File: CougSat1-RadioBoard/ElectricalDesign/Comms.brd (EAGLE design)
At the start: 91.4 x 95.8 mm, 427 parts, among them J1 230mm Antenna, J2 CougSat Card, J3 230mm Antenna, J4 SWD, Q1 CSD25402Q3A, Q10 MMBTA06W, Q11 MMBTA06W, Q12 DMN53D0LDW, Q13 DMP2065UFDB, Q14 MMBTA06W, Q15 CSD25402Q3A, Q16 CSD25402Q3A, Q2 CSD25402Q3A, Q3 CSD25402Q3A, Q4 DMN53D0LDW, Q5 CSD25402Q3A, Q6 CSD25402Q3A, Q7 CSD25402Q3A, Q8 DMN53D0LDW, Q9 DMN53D0LDW, U1 TPS73250, U10 MAAP-011232, U11 LTC2499, U12 LTC2499, U13 LTC2499, U14 LP5907MFX-3.1, U15 TPS73250, U16 AD8137, U17 STM32L496RGT, U18 AD8137, U19 MAAP-011232, U2 LP5907MFX-3.1, U20 ADF4360, U21 HMC545A, U22 AD8515, U23 MAAM-011229, U24 AD8515, U25 MAAM-011229, U26 AD8345, U27 LM2776, U28 AD8348, U29 MCP1501-18, U3 TPS61236, U30 TXS0102DQM, U31 MAAM-011229, U32 AD8515, U33 AD8515, U34 AD8515, U35 TXS0102DQM, U36 ADF4360, U37 AD8515, U38 AD8515, U39 AD8515, U4 AD8346, U40 AD8515, U41 AD8137, U42 AD8137, U43 LP5907MFX-3.1, U44 TPS73250, U5 ADF4360, U6 TPS61089, U7 MAAM-011229, U8 IS25LP016D, U9 IS25LP016D, Y1 20MHz ±2.5ppm, Y2 32.768kHz ±10ppm, Y3 16MHz ±10ppm, Y4 20MHz ±2.5ppm, Y5 20MHz ±2.5ppm

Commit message: Updated mCAD
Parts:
- removed R116, R117, R118: 10kΩ 0.1%, CougsInSpace-Resistors:1608
- removed R119, R120, R121: 1.2kΩ 0.1%, CougsInSpace-Resistors:1608
- removed R122: 0Ω <20mΩ, CougsInSpace-Resistors:1608
- removed R123, R124: 50mΩ 1%, CougsInSpace-Resistors:1608
- removed R125: 1kΩ 0.1%, CougsInSpace-Resistors:1608
- removed R126, R127, R128: 5kΩ 0.1%, CougsInSpace-Resistors:1616
- added RN1, RN5, RN6: 50kΩ 0.1%, CougsInSpace-Resistors:1616
- added RN10, RN2, RN3, RN4, RN7, RN8, RN9: 20kΩ 0.1%, CougsInSpace-Resistors:1616
- added RN11, RN12, RN13: 5kΩ 0.1%, CougsInSpace-Resistors:1616
- R100: value 1kΩ 0.1% -> 10kΩ 0.1%
- R101, R102, R103: value 100kΩ 0.1% -> 10kΩ 0.1%
- R104: value 13.7kΩ 0.1% -> 10kΩ 0.1%
- R105, R106, R107, R108, R66: value 3.3kΩ 0.1% -> 10kΩ 0.1%
- R110, R111: value 10kΩ 0.1% -> 1.2kΩ 0.1%
- R112, R33, R41, R46: value 10kΩ 0.1% -> 0Ω <20mΩ
- R113, R114, R37: value 10kΩ 0.1% -> 50mΩ 1%
- R115: value 10kΩ 0.1% -> 1kΩ 0.1%
- R24, R32: value 50kΩ 0.1% -> 0Ω <20mΩ; device CougsInSpace-Resistors:1616 -> CougsInSpace-Resistors:1608
- R25: value 0Ω <20mΩ -> 4.7kΩ 0.1%
- R26, R29, R30, R36: value 20kΩ 0.1% -> 10kΩ 0.1%; device CougsInSpace-Resistors:1616 -> CougsInSpace-Resistors:1608
- R27: value 4.7kΩ 0.1% -> 50mΩ 1%
- R31: value 50mΩ 1% -> 10kΩ 0.1%
- R35: value 50kΩ 0.1% -> 10kΩ 0.1%; device CougsInSpace-Resistors:1616 -> CougsInSpace-Resistors:1608
- R38, R39: value 20kΩ 0.1% -> 50mΩ 1%; device CougsInSpace-Resistors:1616 -> CougsInSpace-Resistors:1608
- R40: value 20kΩ 0.1% -> 0Ω <20mΩ; device CougsInSpace-Resistors:1616 -> CougsInSpace-Resistors:1608
- R42, R56: value 0Ω <20mΩ -> 3.3kΩ 0.1%
- R43, R50, R51, R67, R81: value 0Ω <20mΩ -> 2kΩ 0.1%
- R44, R87: value 10kΩ 0.1% -> 100kΩ 0.1%
- R45: value 10kΩ 0.1% -> 820kΩ 1%
- R47: value 50mΩ 1% -> 100kΩ 0.1%
- R48: value 50mΩ 1% -> 820kΩ 1%
- R49: value 50mΩ 1% -> 3.3kΩ 0.1%
- R53: value 2kΩ 0.1% -> 1kΩ 0.1%
- R54: value 100kΩ 0.1% -> 13.7kΩ 0.1%
- R55: value 820kΩ 1% -> 2kΩ 0.1%
- R57: value 100kΩ 0.1% -> 0Ω <20mΩ
- R58: value 820kΩ 1% -> 200kΩ 0.1%
- R59: value 3.3kΩ 0.1% -> 49.9Ω 0.1%
- R60: value 2kΩ 0.1% -> 49.9Ω 0.1%
- R61: value 2kΩ 0.1% -> 4.7kΩ 0.1%
- R62: value 3.3kΩ 0.1% -> 0Ω <20mΩ
- R63: value 1kΩ 0.1% -> 2kΩ 0.1%
- R64: value 13.7kΩ 0.1% -> 470Ω 0.5%
- R65, R89, R91: value 2kΩ 0.1% -> 100kΩ 0.1%
- R68: value 200kΩ 0.1% -> 2kΩ 0.1%
- R69, R85: value 49.9Ω 0.1% -> 470Ω 0.5%
- R70: value 49.9Ω 0.1% -> 2kΩ 0.1%
- R71: value 4.7kΩ 0.1% -> 0Ω <20mΩ
- R72: value 0Ω <20mΩ -> 10kΩ 0.1%
- R73, R77: value 2kΩ 0.1% -> 10kΩ 0.1%
- R74: value 470Ω 0.5% -> 10kΩ 0.1%
- R75: value 100kΩ 0.1% -> 49.9Ω 0.1%
- R76: value 10kΩ 0.1% -> 20kΩ 0.5%
- R78: value 2kΩ 0.1% -> 60.4Ω 0.1%
- R79: value 470Ω 0.5% -> 2kΩ 0.1%
- R80: value 2kΩ 0.1% -> 316kΩ 0.1%
- R82: value 10kΩ 0.1% -> 49.9Ω 0.1%
- R83: value 10kΩ 0.1% -> 470Ω 0.5%
- R84: value 10kΩ 0.1% -> 4.7kΩ 0.1%
- R86: value 20kΩ 0.5% -> 200kΩ 0.1%
- R88: value 60.4Ω 0.1% -> 100kΩ 0.1%
- R90: value 316kΩ 0.1% -> 1kΩ 0.1%
- R92: value 49.9Ω 0.1% -> 100kΩ 0.1%
- R93: value 470Ω 0.5% -> 100kΩ 0.1%
- R94: value 4.7kΩ 0.1% -> 13.7kΩ 0.1%
- R95: value 470Ω 0.5% -> 3.3kΩ 0.1%
- R96: value 200kΩ 0.1% -> 3.3kΩ 0.1%
- R97, R98: value 100kΩ 0.1% -> 3.3kΩ 0.1%
- R99: value 100kΩ 0.1% -> 1.2kΩ 0.1%
- moved R63 82.3 mm to (88.3, -16.2)
- moved R80 68.6 mm to (18.3, -25.0), turned to 0 degrees
- moved R67 61.8 mm to (69.1, -17.1)
- moved R100 59.6 mm to (70.0, -38.9), turned to 180 degrees
- moved R82 59.6 mm to (86.9, -25.5), turned to 180 degrees
- moved R57 59.0 mm to (7.50, -12.1), turned to 90 degrees
- moved R92 57.8 mm to (29.5, -31.9), turned to 270 degrees
- moved R73 56.2 mm to (32.2, -19.3), turned to 90 degrees
- moved R95 55.6 mm to (23.7, -34.5)
- moved R75 54.0 mm to (87.4, -20.1)
- moved R33 52.1 mm to (75.7, 10.6), turned to 180 degrees
- moved R83 51.5 mm to (83.3, -26.0), turned to 180 degrees
- moved R104 51.5 mm to (35.4, -40.4), turned to 270 degrees
- moved R114 49.8 mm to (85.2, -42.2), turned to 180 degrees
- moved R42 49.7 mm to (35.9, -1.50), turned to 180 degrees
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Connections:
- net !NRST: now also R62.1; no longer R72.1
- net 3.3V: now also R100.2, R28.2, R29.2, R30.2, R31.2, R36.2, R53.2, R66.2, R72.2; no longer R110.2, R33.2, R34.2, R37.2, R41.2, R46.2, R63.2, R76.2, R82.2
- net 3.3V_1: now also R75.2, R82.2; no longer R85.2, R92.2
- net 3.3V_2: now also R59.2, R60.2; no longer R69.2, R70.2
- net 5.0V: now also RN2.3; no longer R26.3
- net 5.0V_1: now also R63.2; no longer R73.2
- net 5.0V_2: now also R67.2, R81.2; no longer R77.2, R91.2
- net 5.0V_I: now also RN2.4; no longer R26.4
- net 9.0V: now also RN1.4; no longer R24.4
- net 9.0V_0: now also R27.2, RN5.3; no longer R31.2, R32.3
- net 9.0V_1: now also R39.2, R44.2, R47.2, RN6.4; no longer R35.4, R49.2, R54.2, R57.2
- net 9.0V_I: now also RN1.3; no longer R24.3
- net ADC_5.0V: now also RN2.2; no longer R26.2
- net ADC_5.0V_I: now also RN2.1; no longer R26.1
- net ADC_9.0V: now also RN1.1; no longer R24.1
- net ADC_9.0V_0: now also RN5.2; no longer R32.2
- net ADC_9.0V_1: now also RN6.1; no longer R35.1
- net ADC_9.0V_I: now also RN1.2; no longer R24.2
- net ADC_ADCINN-0: now also RN12.4, RN8.1; no longer R127.4, R38.1
- net ADC_ADCINN-1: now also RN13.4, RN3.1; no longer R128.4, R29.1
- net ADC_ADCINN-2: now also RN10.1, RN11.4; no longer R126.4, R40.1
- net ADC_ADCINP-0: now also RN12.3, RN8.2; no longer R127.3, R38.2
- net ADC_ADCINP-1: now also RN13.3, RN3.2; no longer R128.3, R29.2
- net ADC_ADCINP-2: now also RN10.2, RN11.3; no longer R126.3, R40.2
- net ADC_I_5.0V-0N: now also RN4.1; no longer R30.1
- net ADC_I_5.0V-0P: now also RN4.2; no longer R30.2
- net ADC_I_5.0V-1N: now also RN9.1; no longer R39.1
- net ADC_I_5.0V-1P: now also RN9.2; no longer R39.2
- net ADC_I_5.0V-2N: now also RN7.1; no longer R36.1
- net ADC_I_5.0V-P: now also RN7.2; no longer R36.2
- net ADC_I_9.0V_0: now also RN5.1; no longer R32.1
- net ADC_I_9.0V_1: now also RN6.2; no longer R35.2
- net ADC_MUXOUTN-0: now also RN8.4; no longer R38.4
- net ADC_MUXOUTN-1: now also RN3.4; no longer R29.4
- net ADC_MUXOUTN-2: now also RN10.4; no longer R40.4
- net ADC_MUXOUTP-0: now also RN8.3; no longer R38.3
- net ADC_MUXOUTP-1: now also RN3.3; no longer R29.3
- net ADC_MUXOUTP-2: now also RN10.3; no longer R40.3
- net AGND: now also R58.1, R71.1, R73.1, R86.1, R89.1, R91.1, RN11.1, RN11.2, RN12.1, RN12.2, RN13.1, RN13.2; no longer R101.1, R126.1, R126.2, R127.1, R127.2, R128.1, R128.2, R68.1, R81.1, R83.1, R96.1, R99.1
- net AMP_230_I_IN+: now also R51.1, R52.2; no longer R61.1, R62.2
- net AMP_230_I_IN-: now also R55.1, R56.2; no longer R65.1, R66.2
- net AMP_230_Q_IN+: now also R42.2, R43.1; no longer R52.2, R53.1
- net AMP_230_Q_IN-: now also R49.2, R50.1; no longer R59.2, R60.1
- net AMP_700_I_IN+: now also R98.2, R99.1; no longer R108.2, R109.1
- net AMP_700_I_IN-: now also R111.1, R97.2; no longer R107.2, R121.1
- net AMP_700_Q_IN+: now also R110.1, R96.2; no longer R106.2, R120.1
- net AMP_700_Q_IN-: now also R109.1, R95.2; no longer R105.2, R119.1
- net ANTENNA_SW_A: now also R47.1, R48.2; no longer R57.1, R58.2
- net ANTENNA_SW_B: now also R44.1, R45.2; no longer R54.1, R55.2
- net AVDD: now also R74.2; no longer R84.2
- net AVDD_NEG: now also R87.1, R92.1; no longer R102.1, R97.1
- net AVREF: now also R65.2, R77.2, R80.2; no longer R75.2, R87.2, R90.2
- net BOOT0: now also R41.2; no longer R51.2
- net CHASSIS: now also R112.2, R32.2, R40.2; no longer R122.2, R42.2, R50.2
- net CTRL_!RESET: now also R62.2; no longer R72.2
- net DEMOD_700_LOI_N: now also R78.1; no longer R88.1
- net DEMOD_700_LOI_P: now also R78.2; no longer R88.2
- net DEMOD_AMP_ID_IN+: now also R105.1, R106.2; no longer R115.1, R116.2
- net DEMOD_AMP_ID_IN-: now also R107.2, R108.1; no longer R117.2, R118.1
- net DEMOD_AMP_QD_IN+: now also R101.1, R102.2; no longer R111.1, R112.2
- net DEMOD_AMP_QD_IN-: now also R103.2, R104.1; no longer R113.2, R114.1
- net DEMOD_ID: now also R108.2; no longer R118.2
- net DEMOD_ID_N: now also R107.1; no longer R117.1
- net DEMOD_ID_P: now also R106.1; no longer R116.1
- net DEMOD_QD: now also R104.2; no longer R114.2
- net DEMOD_QD_N: now also R103.1; no longer R113.1
- net DEMOD_QD_P: now also R102.1; no longer R112.1
- net DEMOD_VGIN: now also R76.2, R77.1; no longer R86.2, R87.1
- net DGND: now also R115.1, R41.1, R57.1, R71.2, R90.1; no longer R100.1, R125.1, R51.1, R67.1, R81.2
- net FLASH_HOLD-A: now also R28.1; no longer R33.1
- net FLASH_HOLD-B: now also R29.1; no longer R34.1
- net I2C_SCL: now also R30.1; no longer R37.1
- net I2C_SDA: now also R31.1; no longer R41.1
- net I_3.3V-1N: now also R113.1; no longer R123.1
- net I_3.3V-1P: now also R113.2; no longer R123.2
- net I_3.3V-2N: now also R37.1; no longer R47.1
- net I_3.3V-2P: now also R37.2; no longer R47.2
- net I_5.0V-0N: now also RN4.4; no longer R30.4
- net I_5.0V-0P: now also RN4.3; no longer R30.3
- net I_5.0V-1N: now also R114.1, RN9.4; no longer R124.1, R39.4
- net I_5.0V-1P: now also R114.2, RN9.3; no longer R124.2, R39.3
- net I_5.0V-2N: now also R38.1, RN7.4; no longer R36.4, R48.1
- net I_5.0V-2P: now also R38.2, RN7.3; no longer R36.3, R48.2
- net I_9.0V_0: now also R27.1, RN5.4; no longer R31.1, R32.4
- net I_9.0V_1: now also R39.1, RN6.3; no longer R35.3, R49.1
- net JTAG_EN_COMMS: now also R90.2; no longer R100.2
- net LED_C: now also R115.2; no longer R125.2
- net MOD_230_ID: now also R56.1; no longer R66.1
- net MOD_230_ID_N: now also R51.2; no longer R61.2
- net MOD_230_ID_P: now also R55.2; no longer R65.2
- net MOD_230_QD: now also R49.1; no longer R59.1
- net MOD_230_QD_N: now also R43.2; no longer R53.2
- net MOD_230_QD_P: now also R50.2; no longer R60.2
- net MOD_700_ID: now also R97.1; no longer R107.1
- net MOD_700_ID_N: now also R99.2; no longer R109.2
- net MOD_700_ID_P: now also R111.2; no longer R121.2
- net MOD_700_QD: now also R95.1; no longer R105.1
- net MOD_700_QD_N: now also R110.2; no longer R120.2
- net MOD_700_QD_P: now also R109.2; no longer R119.2
- net PA_230_BIAS: now also R89.2; no longer R99.2
- net PA_230_BIAS_AMPIN-0: now also R87.2; no longer R97.2
- net PA_230_BIAS_AMPIN-1: now also R88.2; no longer R98.2
- net PA_230_BIAS_AMPOUT-0: now also R88.1; no longer R98.1
- net PA_700_BIAS: now also R91.2; no longer R101.2
- net PA_700_BIAS_AMPIN-0: now also R92.2; no longer R102.2
- net PA_700_BIAS_AMPIN-1: now also R93.2; no longer R103.2
- net PA_700_BIAS_AMPOUT-0: now also R93.1; no longer R103.1
- net PC_DEMOD: now also R34.1; no longer R44.1
- net PC_DEMOD_LV: now also R72.1; no longer R82.1
- net PC_LDO_3.3V: now also R100.1; no longer R110.1
- net PC_MOD_230: now also R26.1; no longer R28.1
- net PC_MOD_230_LV: now also R36.1; no longer R46.1
- net PC_MOD_700: now also R35.1; no longer R45.1
- net PC_MOD_700_LV: now also R66.1; no longer R76.1
- net PC_VHIGH: now also R26.2, R34.2, R35.2; no longer R28.2, R44.2, R45.2
- net PGND: now also R112.1, R25.1, R32.1, R33.2, R40.1, R45.1, R46.2, R48.1, R57.2; no longer R122.1, R27.1, R42.1, R43.2, R50.1, R55.1, R56.2, R58.1, R67.2
- net PREAMP_700_BIAS: now also R63.1, R70.2; no longer R73.1, R80.2
- net REG_FB-9: now also R24.2; no longer R25.2
- net REG_FB_RES-LOW-9: now also R24.1, R25.2; no longer R25.1, R27.2
- net RFCLK_CP-DEMOD: now also R54.2; no longer R64.2
- net RFCLK_CP-MOD: now also R94.2; no longer R104.2
- net RFCLK_L1-DEMOD: now also R64.2; no longer R74.2
- net RFCLK_L1-MOD: now also R83.2; no longer R93.2
- net RFCLK_L2-DEMOD: now also R69.2; no longer R79.2
- net RFCLK_L2-MOD: now also R85.2; no longer R95.2
- net RFCLK_OUT-DEMOD_N: now also R60.1; no longer R70.1
- net RFCLK_OUT-DEMOD_P: now also R59.1; no longer R69.1
- net RFCLK_OUT-MOD_N: now also R82.1; no longer R92.1
- net RFCLK_OUT-MOD_P: now also R75.1; no longer R85.1
- net RFCLK_RSET-DEMOD: now also R61.2; no longer R71.2
- net RFCLK_RSET-MOD: now also R84.2; no longer R94.2
- net RFCLK_VTUNE_FILTER-DEMOD: now also R54.1; no longer R64.1
- net RFCLK_VTUNE_FILTER-MOD: now also R94.1; no longer R104.1
- net RFGND-0: now also R33.1; no longer R43.1
- net RFGND-1: now also R46.1, R61.1, R64.1, R68.1, R69.1, R70.1, R76.1, R83.1, R84.1, R85.1; no longer R56.1, R71.1, R74.1, R78.1, R80.1, R86.1, R89.1, R93.1, R94.1, R95.1
- net RX_LNA_BIAS-0: now also R67.1, R68.2; no longer R77.1, R78.2
- net RX_LNA_BIAS-1: now also R79.2, R81.1; no longer R89.2, R91.1
- net SWD_VSENSE: now also R53.1; no longer R63.1
- net VREF_CM_IN: now also R101.2, R105.2, R42.1, R96.1, R98.1; no longer R106.1, R108.1, R111.2, R115.2, R62.1
- net VREF_CM_IN_AMP_IN: now also R73.2, R74.1; no longer R83.2, R84.1
- net VREF_CM_OUT_AMP_IN_230: now also R58.2, R65.1; no longer R68.2, R75.1
- net VREF_CM_OUT_AMP_IN_700: now also R80.1, R86.2; no longer R90.1, R96.2

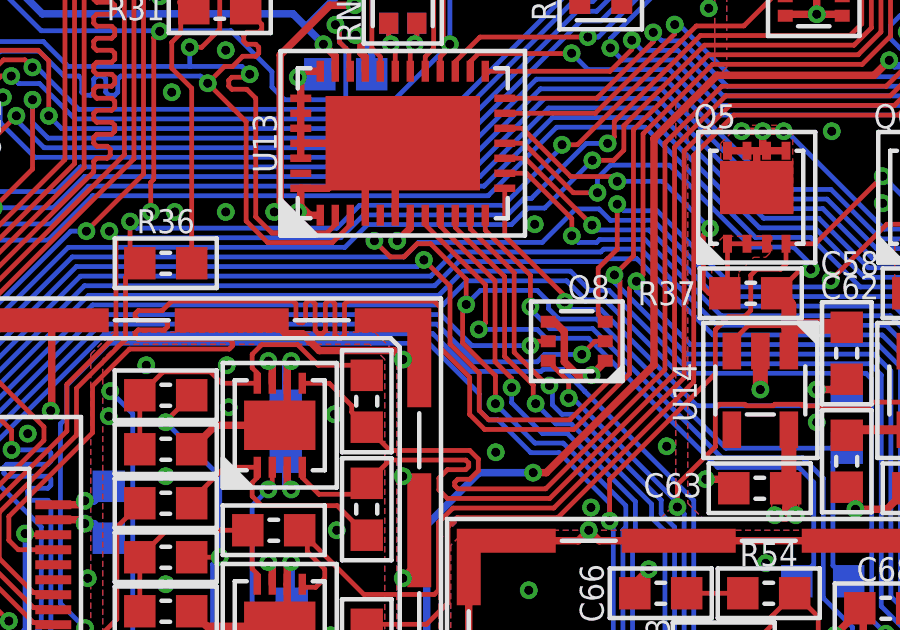
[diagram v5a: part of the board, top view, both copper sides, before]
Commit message: Wrote Power Supplies and µController Tests
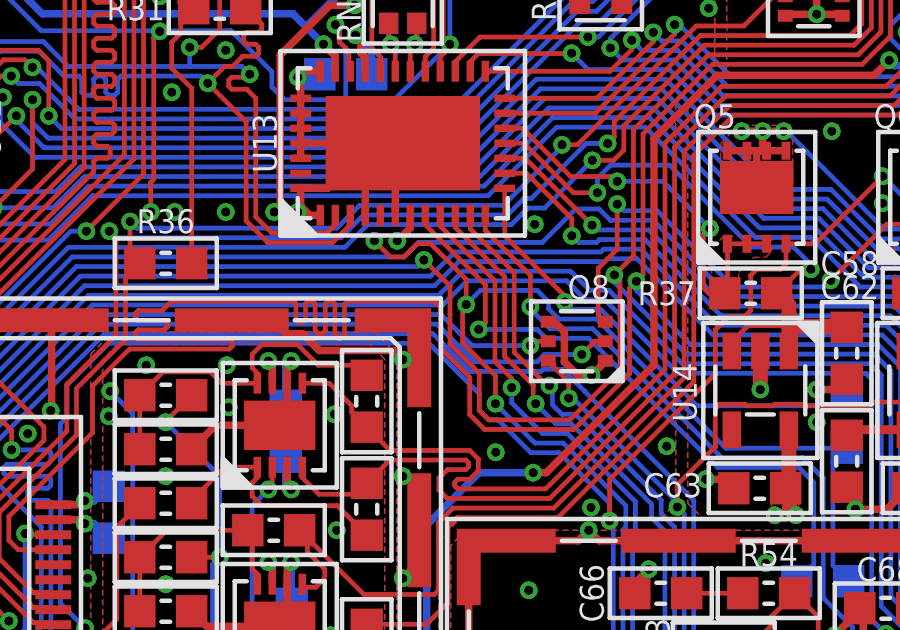
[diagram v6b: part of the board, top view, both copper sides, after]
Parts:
- R7: value 330kΩ 1% -> 316kΩ 0.1%
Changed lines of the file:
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@@
 <drawing>
 <settings>
-<setting alwaysvectorfont="yes"/>
+<setting alwaysvectorfont="no"/>
 <setting verticaltext="up"/>
 </settings>
@@
 <attribute name="TEMP" value="25ppm/°C" x="-122.71" y="161.2" size="1.778" layer="27" rot="R180" display="off"/>
 </element>
-<element name="R7" library="CougsInSpace-Resistors" package="1608" value="330kΩ 1%" x="38.1" y="38.1" smashed="yes">
+<element name="R7" library="CougsInSpace-Resistors" package="1608" value="316kΩ 0.1%" x="38.1" y="38.1" smashed="yes">
 <attribute name="NAME" x="45" y="41.1" size="0.8" layer="25" font="vector" ratio="15" align="center"/>
 <attribute name="PACKAGE" value="1608" x="148.59" y="-135.89" size="1.778" layer="27" display="off"/>
-<attribute name="POWER" value="1/10W" x="148.59" y="-135.89" size="1.778" layer="27" display="off"/>
-<attribute name="SKU" value="21-3303" x="148.59" y="-135.89" size="1.778" layer="27" display="off"/>
-<attribute name="TEMP" value="100ppm/°C" x="148.59" y="-135.89" size="1.778" layer="27" display="off"/>
+<attribute name="POWER" value="1/8W" x="148.59" y="-135.89" size="1.778" layer="27" display="off"/>
+<attribute name="SKU" value="21-3163" x="148.59" y="-135.89" size="1.778" layer="27" display="off"/>
+<attribute name="TEMP" value="25ppm/°C" x="148.59" y="-135.89" size="1.778" layer="27" display="off"/>
 </element>
 <element name="R58" library="CougsInSpace-Resistors" package="1608" value="200kΩ 0.1%" x="34.3" y="-13.9" smashed="yes" rot="R270">
@@
 <wire x1="49.37" y1="-2.32" x2="51.04" y2="-0.65" width="0.16" layer="1"/>
 <wire x1="51.04" y1="-0.65" x2="51.04" y2="2.325" width="0.16" layer="1"/>
-<wire x1="45.375" y1="2.14" x2="45.375" y2="0.21" width="0.16" layer="1"/>
+<wire x1="45.375" y1="2.14" x2="45.375" y2="1.2" width="0.16" layer="1"/>
+<wire x1="45.375" y1="1.2" x2="45.375" y2="0.21" width="0.16" layer="1"/>
 <wire x1="46.35" y1="-2.005" x2="46.665" y2="-2.32" width="0.16" layer="1"/>
 <wire x1="45.375" y1="0.21" x2="46.35" y2="-0.765" width="0.16" layer="1"/>

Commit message: Wrote RF Chain Testing and Added mCAD to Full Assembly
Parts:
- U14, U2, U43: value LP5907MFX-3.1 -> LP5907MFX-3.3
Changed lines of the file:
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@@
 <?xml version="1.0" encoding="utf-8"?>
 <!DOCTYPE eagle SYSTEM "eagle.dtd">
-<eagle version="9.2.2">
+<eagle version="9.3.0">
 <drawing>
 <settings>
@@
 <attribute name="SKU" value="65-0009" x="221.12" y="52.94" size="1.778" layer="27" rot="R90" display="off"/>
 </element>
-<element name="U2" library="CougsInSpace-IC-Power" package="SOT23-5" value="LP5907MFX-3.1" x="63.3" y="41.5" smashed="yes">
+<element name="U2" library="CougsInSpace-IC-Power" package="SOT23-5" value="LP5907MFX-3.3" x="63.3" y="41.5" smashed="yes">
 <attribute name="IMAX" value="250mA" x="134.42" y="-105.82" size="1.778" layer="27" display="off"/>
 <attribute name="NAME" x="63.3" y="43.9" size="0.8" layer="25" font="vector" ratio="15" align="center"/>
-<attribute name="SKU" value="60-0009" x="134.42" y="-105.82" size="1.778" layer="27" display="off"/>
+<attribute name="SKU" value="60-0013" x="134.42" y="-105.82" size="1.778" layer="27" display="off"/>
 <attribute name="VDO" value="&lt;250mV" x="134.42" y="-105.82" size="1.778" layer="27" display="off"/>
-<attribute name="VOUT" value="3.1V 2%" x="134.42" y="-105.82" size="1.778" layer="27" display="off"/>
+<attribute name="VOUT" value="3.3V 2%" x="134.42" y="-105.82" size="1.778" layer="27" display="off"/>
 </element>
 <element name="U5" library="CougsInSpace-RF" package="QFN-24-4040" value="ADF4360" x="69.6" y="33.3" smashed="yes" rot="R180">
@@
 <attribute name="SKU" value="08-0002" x="169.68" y="-164.72" size="1.778" layer="27" display="off"/>
 </element>
-<element name="U14" library="CougsInSpace-IC-Power" package="SOT23-5" value="LP5907MFX-3.1" x="55.72" y="-1.34" smashed="yes" rot="R270">
+<element name="U14" library="CougsInSpace-IC-Power" package="SOT23-5" value="LP5907MFX-3.3" x="55.72" y="-1.34" smashed="yes" rot="R270">
 <attribute name="IMAX" value="250mA" x="-91.6" y="-138.5" size="1.778" layer="27" rot="R270" display="off"/>
 <attribute name="NAME" x="53.2" y="-1.4" size="0.8" layer="25" font="vector" ratio="15" rot="R270" align="center"/>
-<attribute name="SKU" value="60-0009" x="-91.6" y="-138.5" size="1.778" layer="27" rot="R270" display="off"/>
+<attribute name="SKU" value="60-0013" x="-91.6" y="-138.5" size="1.778" layer="27" rot="R270" display="off"/>
 <attribute name="VDO" value="&lt;250mV" x="-91.6" y="-138.5" size="1.778" layer="27" rot="R270" display="off"/>
-<attribute name="VOUT" value="3.1V 2%" x="-91.6" y="-138.5" size="1.778" layer="27" rot="R270" display="off"/>
+<attribute name="VOUT" value="3.3V 2%" x="-91.6" y="-138.5" size="1.778" layer="27" rot="R270" display="off"/>
 </element>
 <element name="U17" library="CougsInSpace-IC-µController" package="QFP-64-1010" value="STM32L496RGT" x="26.4" y="-8.9" smashed="yes">
@@
 <attribute name="SKU" value="61-0004" x="169.91" y="-116.85" size="1.778" layer="27" display="off"/>
 </element>
-<element name="U43" library="CougsInSpace-IC-Power" package="SOT23-5" value="LP5907MFX-3.1" x="76.8" y="-41.9" smashed="yes" rot="R90">
+<element name="U43" library="CougsInSpace-IC-Power" package="SOT23-5" value="LP5907MFX-3.3" x="76.8" y="-41.9" smashed="yes" rot="R90">
 <attribute name="IMAX" value="250mA" x="224.12" y="100.34" size="1.778" layer="27" rot="R90" display="off"/>
 <attribute name="NAME" x="50.5" y="-41.1" size="0.8" layer="25" font="vector" ratio="15" rot="R270" align="center"/>
-<attribute name="SKU" value="60-0009" x="224.12" y="100.34" size="1.778" layer="27" rot="R90" display="off"/>
+<attribute name="SKU" value="60-0013" x="224.12" y="100.34" size="1.778" layer="27" rot="R90" display="off"/>
 <attribute name="VDO" value="&lt;250mV" x="224.12" y="100.34" size="1.778" layer="27" rot="R90" display="off"/>
-<attribute name="VOUT" value="3.1V 2%" x="224.12" y="100.34" size="1.778" layer="27" rot="R90" display="off"/>
+<attribute name="VOUT" value="3.3V 2%" x="224.12" y="100.34" size="1.778" layer="27" rot="R90" display="off"/>
 </element>
 <element name="U35" library="CougsInSpace-IC-Comms" package="X2SON-8" value="TXS0102DQM" x="8.5" y="-29" smashed="yes" rot="R90">
